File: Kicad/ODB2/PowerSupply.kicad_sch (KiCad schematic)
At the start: 54 parts, among them J2 Batt4v2, J3 Batt7V4, Q3 PJA3411_R1_00001, U2 TPS61201DRCR, U3 LM1085-5.0, U8 MCP1727-1802xMF

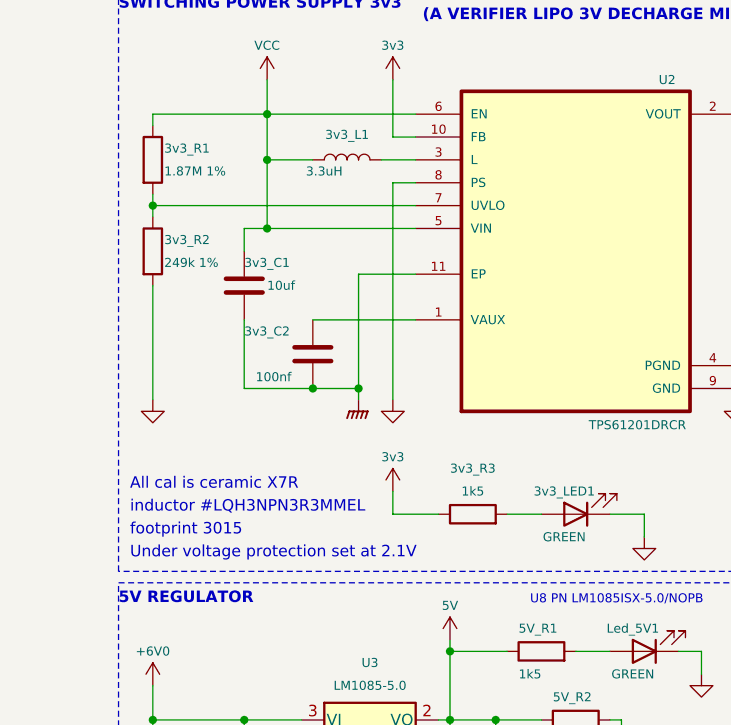
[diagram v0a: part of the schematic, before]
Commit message: fix 3v3_R1 + amp pyros dual channel
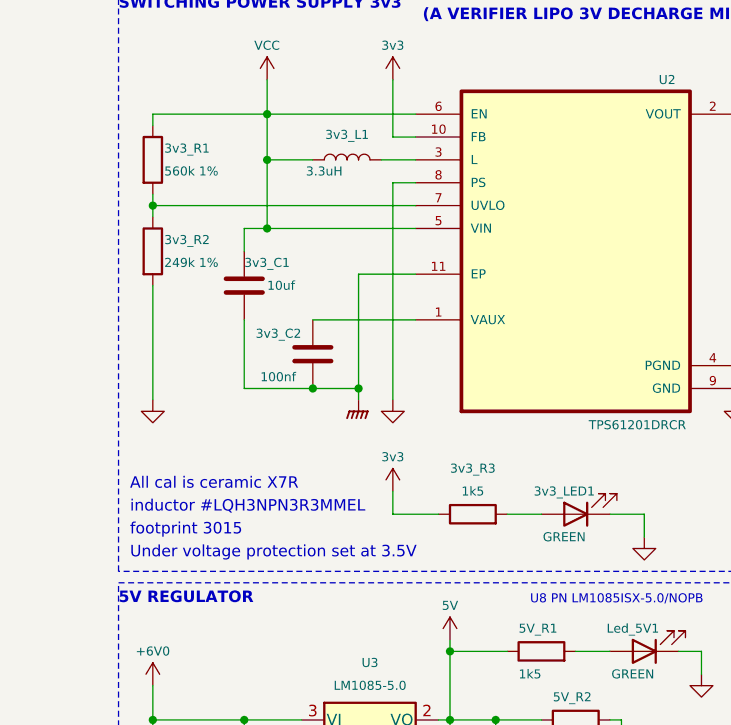
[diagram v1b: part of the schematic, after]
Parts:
- 3v3_R1: value 1.87M 1% -> 560k 1%
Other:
- note added: "Under voltage protection set at 3.5V"
- note removed: "Under voltage protection set at 2.1V"
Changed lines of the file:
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@@
 		)
 	)
-	(text "Under voltage protection set at 2.1V"
+	(text "Under voltage protection set at 3.5V"
 		(exclude_from_sim no)
 		(at 16.51 85.09 0)
@@
 			)
 		)
-		(property "Value" "1.87M 1%"
+		(property "Value" "560k 1%"
 			(at 20.32 41.91 0)
 			(effects
@@
 		(dnp no)
 		(property "Reference" "3v3_C2"
-			(at 29.21 59.69 0)
+			(at 30.48 59.944 0)
 			(effects
 				(font
@@
 		)
 		(property "Value" "100nf"
-			(at 30.48 64.77 0)
-			(effects
-				(font
+			(at 30.988 64.77 0)
+			(effects
+				(font

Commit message: fix amp
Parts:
- 3v3_R1: value 560k 1% -> 3M 1%
- renumbered LED_7v4Enable to LED_7v4Enable1
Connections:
- net +6V0 is gone; now on net +7V4: 5V_C1.1, 5V_C2.1, U3.3 (VI)
- net 3v3 is gone; now on net +3V3: 3v3_C3.1, 3v3_C4.1, 3v3_R3.1, U2.10 (FB), U2.2 (VOUT)
- net 4v2 renamed +3V7
- net 5V renamed +5V
- net 7C4 renamed +7C4
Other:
- note added: "Under voltage protection set at 3.27V"
- note removed: "(A VERIFIER LIPO 3V DECHARGE MINIMAL)"
- note removed: "Under voltage protection set at 3.5V"
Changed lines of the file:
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@@
 		)
 	)
-	(text "Under voltage protection set at 3.5V"
+	(text "Under voltage protection set at 3.27V"
 		(exclude_from_sim no)
 		(at 16.51 85.09 0)
@@
 		)
 	)
-	(text "(A VERIFIER LIPO 3V DECHARGE MINIMAL)"
-		(exclude_from_sim no)
-		(at 49.022 25.4 0)
-		(effects
-			(font
-				(size 1.27 1.27)
-				(thickness 0.254)
-				(bold yes)
-			)
-			(justify left bottom)
-		)
-	)
 	(text "4v2 Input"
 		(exclude_from_sim no)
@@
 			)
 		)
-		(property "Value" "560k 1%"
+		(property "Value" "3M 1%"
 			(at 20.32 41.91 0)
 			(effects
@@
 			)
 		)
-		(property "Value" "3v3"
+		(property "Value" "+3V3"
 			(at 90.17 27.94 0)
 			(effects
@@
 			)
 		)
-		(property "Value" "4v2"
+		(property "Value" "+3V7"
 			(at 49.53 129.54 0)
 			(effects
@@
 			)
 		)
-		(property "Value" "5V"
+		(property "Value" "+5V"
 			(at 52.07 90.17 0)
 			(effects
@@
 			)
 		)
-		(property "Value" "7C4"
+		(property "Value" "+7C4"
 			(at 241.3 22.86 0)
 			(effects
@@
 		)
 		(property "Value" "+1V8"
-			(at 89.662 169.164 0)
+			(at 90.17 170.18 0)
 			(effects
 				(font
@@
 		(on_board yes)
 		(dnp no)
-		(property "Reference" "LED_7v4Enable"
+		(property "Reference" "LED_7v4Enable1"
 			(at 208.28 72.39 0)
 			(effects
@@
 			(project "ODB2"
 				(path "/4b06c5d1-aa8b-48ed-8972-b43a60cfab78/a0dfa29e-ccca-4096-8481-c7e33c67aac5"
-					(reference "LED_7v4Enable")
+					(reference "LED_7v4Enable1")
 					(unit 1)
 				)
@@
 			)
 		)
-		(property "Value" "3v3"
+		(property "Value" "+3V3"
 			(at 45.72 73.66 0)
 			(effects
@@
 			)
 		)
-		(property "Value" "3v3"
+		(property "Value" "+3V3"
 			(at 45.72 27.94 0)
 			(effects
@@
 		)
 		(property "Value" "+3V3"
-			(at 21.336 167.894 0)
+			(at 21.59 167.894 0)
 			(effects
 				(font
@@
 			)
 		)
-		(property "Value" "+6V0"
+		(property "Value" "+7V4"
 			(at 19.05 95.25 0)
 			(effects
@@
 			)
 		)
-		(property "Value" "4v2"
+		(property "Value" "+3V7"
 			(at 90.17 125.73 0)
 			(effects

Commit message: Final fixes
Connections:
- net 4v2_An renamed 3v7_An
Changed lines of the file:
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@@
 		)
 	)
-	(global_label "4v2_An"
+	(global_label "3v7_An"
 		(shape input)
 		(at 30.48 144.78 180)

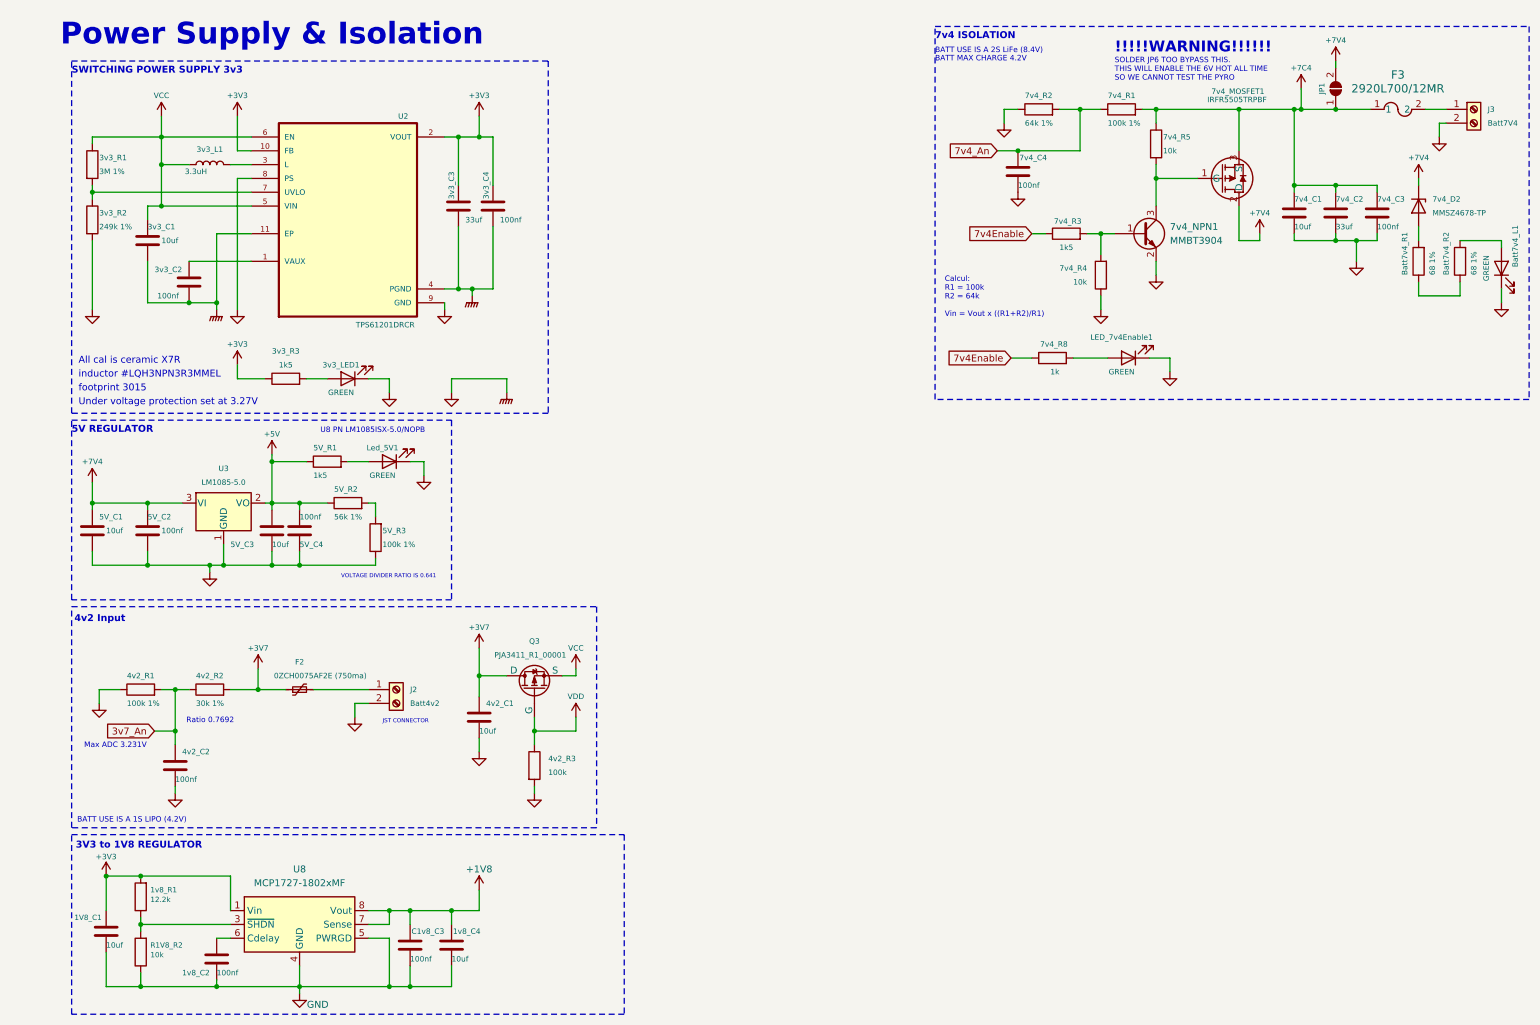
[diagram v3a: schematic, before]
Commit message: fix Labels + fix STM32 projet pinout
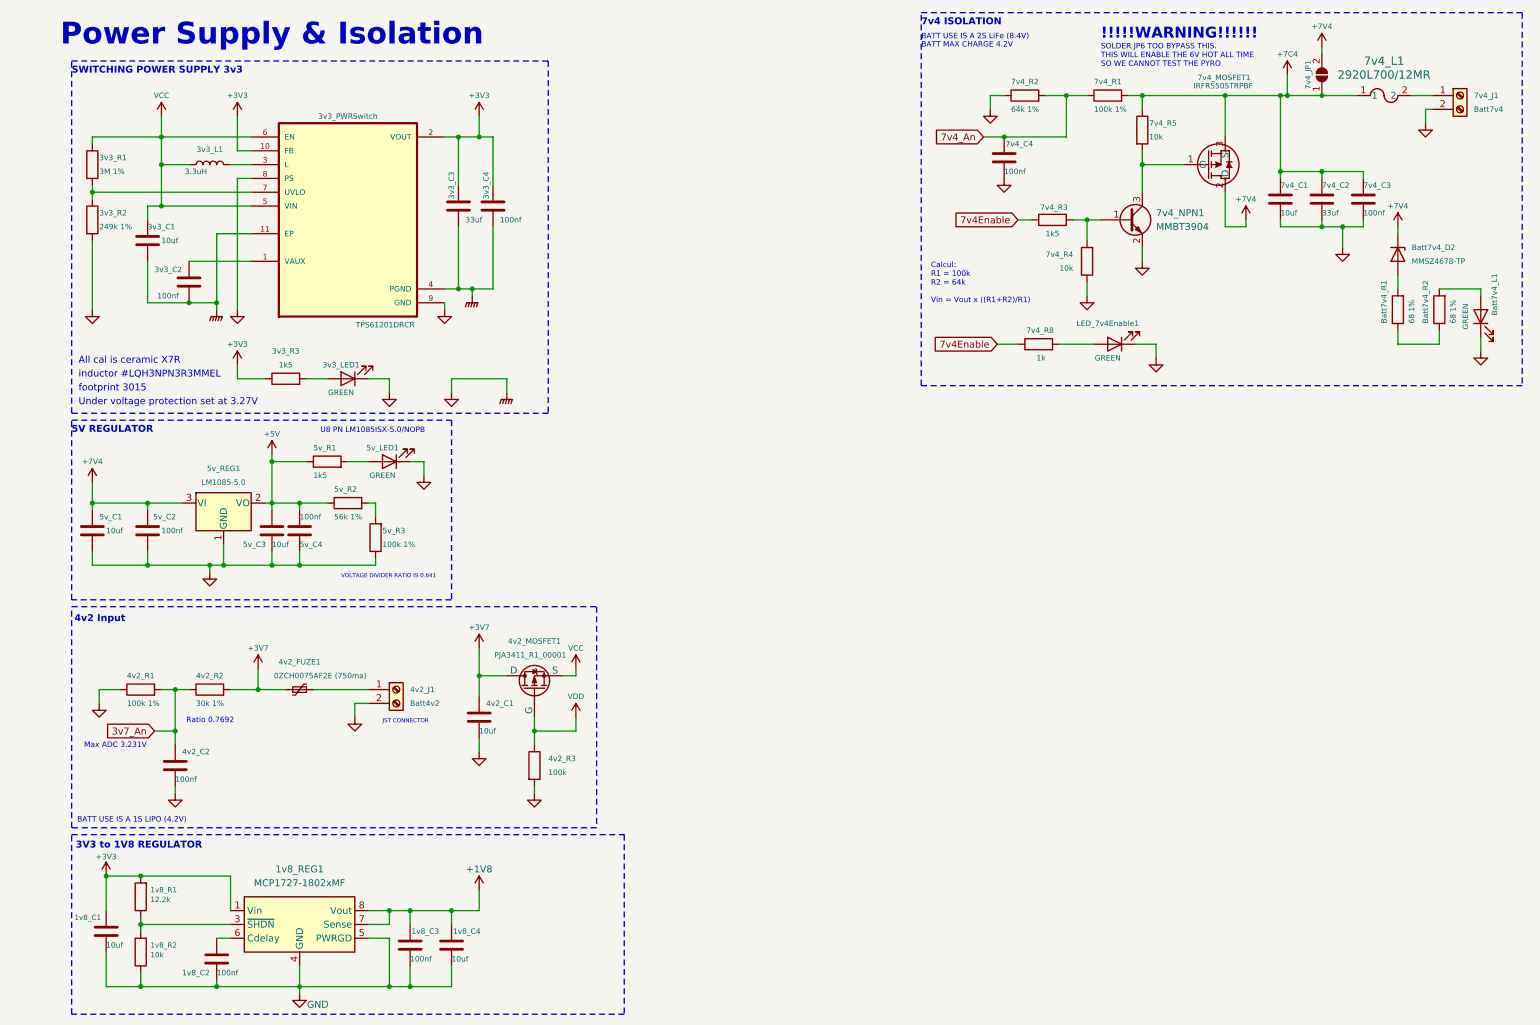
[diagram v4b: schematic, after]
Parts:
- 7v4_J1: renamed from J3; value Batt7V4 -> Batt7v4
- renumbered 1V8_C1 to 1v8_C1, C1v8_C3 to 1v8_C3, R1V8_R2 to 1v8_R2, U8 to 1v8_REG1, U2 to 3v3_PWRSwitch, F2 to 4v2_FUZE1, J2 to 4v2_J1, Q3 to 4v2_MOSFET1, 5V_C1 to 5v_C1, 5V_C2 to 5v_C2, 5V_C3 to 5v_C3, 5V_C4 to 5v_C4, Led_5V1 to 5v_LED1, 5V_R1 to 5v_R1, 5V_R2 to 5v_R2, 5V_R3 to 5v_R3, U3 to 5v_REG1, JP1 to 7v4_JP1, F3 to 7v4_L1, 7v4_D2 to Batt7v4_D2
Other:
- moved on the sheet: 7v4_C1, 7v4_C2, 7v4_C3, 7v4_C4, 7v4_J1, 7v4_JP1, 7v4_L1, 7v4_MOSFET1, 7v4_NPN1, 7v4_R1, 7v4_R2, 7v4_R3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

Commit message: Minor fix et début layout STM et sensors
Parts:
- renumbered 3v3_PWRSwitch to 3v3_PWRSwitch1
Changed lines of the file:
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@@
 		(on_board yes)
 		(dnp no)
-		(property "Reference" "3v3_PWRSwitch"
+		(property "Reference" "3v3_PWRSwitch1"
 			(at 66.04 31.75 0)
 			(effects
@@
 			(project "ODB2"
 				(path "/4b06c5d1-aa8b-48ed-8972-b43a60cfab78/a0dfa29e-ccca-4096-8481-c7e33c67aac5"
-					(reference "3v3_PWRSwitch")
+					(reference "3v3_PWRSwitch1")
 					(unit 1)
 				)

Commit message: Placements composants pcb #1
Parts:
- removed 5v_R2: 56k 1%, Resistor_SMD:R_0805_2012Metric, symbol Device:R
- removed 5v_R3: 100k 1%, Resistor_SMD:R_0805_2012Metric, symbol Device:R
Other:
- note removed: "VOLTAGE DIVIDER RATIO IS 0.641"
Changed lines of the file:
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@@
 	)
 	(junction
-		(at 57.15 114.3)
-		(diameter 0)
-		(color 0 0 0 0)
-	)
-	(junction
-		(at 57.15 102.87)
-		(diameter 0)
-		(color 0 0 0 0)
-	)
-	(junction
 		(at 198.12 27.94)
 		(diameter 0)
@@
 	(wire
 		(pts
-			(xy 71.12 102.87) (xy 71.12 105.41)
-		)
-		(stroke
-			(width 0)
-			(type default)
-		)
-	)
-	(wire
-		(pts
 			(xy 29.21 114.3) (xy 40.64 114.3)
 		)
@@
 	(wire
 		(pts
-			(xy 57.15 114.3) (xy 71.12 114.3)
-		)
-		(stroke
-			(width 0)
-			(type default)
-		)
-	)
-	(wire
-		(pts
 			(xy 201.93 54.61) (xy 201.93 50.8)
 		)
@@
 	(wire
 		(pts
-			(xy 69.85 102.87) (xy 71.12 102.87)
-		)
-		(stroke
-			(width 0)
-			(type default)
-		)
-	)
-	(wire
-		(pts
 			(xy 50.8 102.87) (xy 52.07 102.87)
 		)
@@
 	(wire
 		(pts
-			(xy 57.15 102.87) (xy 62.23 102.87)
-		)
-		(stroke
-			(width 0)
-			(type default)
-		)
-	)
-	(wire
-		(pts
 			(xy 34.29 147.32) (xy 34.29 144.78)
 		)
@@
 	(wire
 		(pts
-			(xy 71.12 114.3) (xy 71.12 113.03)
-		)
-		(stroke
-			(width 0)
-			(type default)
-		)
-	)
-	(wire
-		(pts
 			(xy 52.07 102.87) (xy 57.15 102.87)
 		)
@@
 		)
 	)
-	(text "VOLTAGE DIVIDER RATIO IS 0.641"
-		(exclude_from_sim no)
-		(at 64.77 116.84 0)
-		(effects
-			(font
-				(size 0.75 0.75)
-			)
-			(justify left bottom)
-		)
-	)
 	(text "BATT MAX CHARGE 4.2V"
 		(exclude_from_sim no)
@@
 	)
 	(symbol
-		(lib_id "Device:R")
-		(at 66.04 102.87 90)
-		(unit 1)
-		(exclude_from_sim no)
-		(in_bom yes)
-		(on_board yes)
-		(dnp no)
-		(property "Reference" "5v_R2"
-			(at 63.5 100.33 90)
-			(effects
-				(font
-					(size 1 1)
-				)
-				(justify right)
-			)
-		)
-		(property "Value" "56k 1%"
-			(at 63.5 105.41 90)
-			(effects
-				(font
-					(size 1 1)
-				)
-				(justify right)
-			)
-		)
-		(property "Footprint" "Resistor_SMD:R_0805_2012Metric"
-			(at 66.04 104.648 90)
-			(effects
-				(font
-					(size 1 1)
-				)
-				(hide yes)
-			)
-		)
-		(property "Datasheet" "~"
-			(at 66.04 102.87 0)
-			(effects
-				(font
-					(size 1 1)
-				)
-				(hide yes)
-			)
-		)
-		(property "Description" ""
-			(at 66.04 102.87 0)
-			(effects
-				(font
-					(size 1.27 1.27)
-				)
-				(hide yes)
-			)
-		)
-		(pin "1"
-		)
-		(pin "2"
-		)
-		(instances
-			(project "ODB2"
-				(path "/4b06c5d1-aa8b-48ed-8972-b43a60cfab78/a0dfa29e-ccca-4096-8481-c7e33c67aac5"
-					(reference "5v_R2")
-					(unit 1)
-				)
-			)
-		)
-	)
-	(symbol
 		(lib_id "power:+12C")
 		(at 238.76 24.13 0)
@@
 					(unit 1)
 				)
-			)
-		)
-	)
-	(symbol
-		(lib_id "Device:R")
-		(at 71.12 109.22 180)
-		(unit 1)
-		(exclude_from_sim no)
-		(in_bom yes)
-		(on_board yes)
-		(dnp no)
-		(property "Reference" "5v_R3"
-			(at 72.39 107.95 0)
-			(effects
-				(font
-					(size 1 1)
-				)
-				(justify right)
-			)
-		)
-		(property "Value" "100k 1%"
-			(at 72.39 110.49 0)
-			(effects
-				(font
-					(size 1 1)
-				)
-				(justify right)
-			)
-		)
-		(property "Footprint" "Resistor_SMD:R_0805_2012Metric"
-			(at 72.898 109.22 90)
-			(effects
-				(font
-					(size 1 1)
-				)
-				(hide yes)
-			)
-		)
-		(property "Datasheet" "~"
-			(at 71.12 109.22 0)
-			(effects
-				(font
-					(size 1 1)
-				)
-				(hide yes)
-			)
-		)
-		(property "Description" ""
-			(at 71.12 109.22 0)
-			(effects
-				(font
-					(size 1.27 1.27)
-				)
-				(hide yes)
-			)
-		)
-		(pin "1"
-		)
-		(pin "2"
-		)
-		(instances
-			(project "ODB2"
-				(path "/4b06c5d1-aa8b-48ed-8972-b43a60cfab78/a0dfa29e-ccca-4096-8481-c7e33c67aac5"
-					(reference "5v_R3")
-					(unit 1)
-				)

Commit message: Fix somes issue
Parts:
- 1v8_C1, 1v8_C2, 1v8_C3, 1v8_C4, 3v3_C1, 3v3_C2, 3v3_C3, 3v3_C4, 5v_C1, 5v_C2, 5v_C3, 5v_C4, 7v4_C4: footprint Capacitor_SMD:C_0805_2012Metric -> Capacitor_SMD:C_0603_1608Metric
- 1v8_R1, 1v8_R2, 3v3_R1, 3v3_R2, 3v3_R3, 5v_R1, 7v4_R1, 7v4_R2, 7v4_R3, 7v4_R4, 7v4_R5, 7v4_R8, Batt7v4_R1, Batt7v4_R2: footprint Resistor_SMD:R_0805_2012Metric -> Resistor_SMD:R_0603_1608Metric
- 3v3_LED1, 5v_LED1, Batt7v4_L1, LED_7v4Enable1: footprint LED_SMD:LED_0805_2012Metric -> LED_SMD:LED_0603_1608Metric
- 3v7_C1: renamed from 4v2_C1; footprint Capacitor_SMD:C_0805_2012Metric -> Capacitor_SMD:C_0603_1608Metric
- 3v7_C2: renamed from 4v2_C2; footprint Capacitor_SMD:C_0805_2012Metric -> Capacitor_SMD:C_0603_1608Metric
- 3v7_R1: renamed from 4v2_R1; footprint Resistor_SMD:R_0805_2012Metric -> Resistor_SMD:R_0603_1608Metric
- 3v7_R2: renamed from 4v2_R2; footprint Resistor_SMD:R_0805_2012Metric -> Resistor_SMD:R_0603_1608Metric
- 3v7_R3: renamed from 4v2_R3; footprint Resistor_SMD:R_0805_2012Metric -> Resistor_SMD:R_0603_1608Metric
- 7v4_C1, 7v4_C2, 7v4_C3: footprint Capacitor_SMD:C_1206_3216Metric -> Capacitor_SMD:C_0603_1608Metric
- renumbered 4v2_FUZE1 to 3v7_FUZE1, 4v2_J1 to 3v7_J1, 4v2_MOSFET1 to 3v7_MOSFET1
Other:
- note added: "BATT MAX CHARGE 8.4V"
- note added: "BATT USE IS A 1S LIPO (3.7V)"
- note added: "BATT USE IS A 2S LiFe (7.4V)"
- note added: "Solder JP6 to bypass. This enables 7.4V permanently but disables pyro testing."
- note removed: "BATT USE IS A 1S LIPO (4.2V)"
- note removed: "BATT USE IS A 2S LiFe (8.4V)"
- note removed: "SOLDER JP6 TOO BYPASS THIS. THIS WILL ENABLE THE 6V HOT ALL TIME SO WE CANNOT TEST THE PYRO"
- moved on the sheet: 7v4_C4

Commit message: Updated pcb
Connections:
- net +7C4: no longer names the net of 7v4_C1.1, 7v4_C2.1, 7v4_C3.1, 7v4_JP1.1 (A), 7v4_L1.1, 7v4_MOSFET1.3 (S), 7v4_R1.2, 7v4_R5.1
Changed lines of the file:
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@@
 	)
 	(junction
-		(at 238.76 27.94)
-		(diameter 0)
-		(color 0 0 0 0)
-	)
-	(junction
 		(at 88.9 63.5)
 		(diameter 0)
@@
 	(wire
 		(pts
-			(xy 238.76 24.13) (xy 238.76 27.94)
-		)
-		(stroke
-			(width 0)
-			(type default)
-		)
-	)
-	(wire
-		(pts
 			(xy 259.08 73.66) (xy 259.08 71.12)
 		)
@@
 	(wire
 		(pts
-			(xy 238.76 27.94) (xy 245.11 27.94)
-		)
-		(stroke
-			(width 0)
-			(type default)
-		)
-	)
-	(wire
-		(pts
 			(xy 19.05 46.99) (xy 19.05 45.72)
 		)
@@
 	(wire
 		(pts
-			(xy 237.49 27.94) (xy 238.76 27.94)
+			(xy 237.49 27.94) (xy 245.11 27.94)
 		)
 		(stroke
@@
 					(unit 1)
 				)
-			)
-		)
-	)
-	(symbol
-		(lib_id "power:+12C")
-		(at 238.76 24.13 0)
-		(unit 1)
-		(exclude_from_sim no)
-		(in_bom yes)
-		(on_board yes)
-		(dnp no)
-		(property "Reference" "#PWR028"
-			(at 238.76 27.94 0)
-			(effects
-				(font
-					(size 1 1)
-				)
-				(hide yes)
-			)
-		)
-		(property "Value" "+7C4"
-			(at 238.76 20.32 0)
-			(effects
-				(font
-					(size 1 1)
-				)
-			)
-		)
-		(property "Footprint" ""
-			(at 238.76 24.13 0)
-			(effects
-				(font
-					(size 1 1)
-				)
-				(hide yes)
-			)
-		)
-		(property "Datasheet" ""
-			(at 238.76 24.13 0)
-			(effects
-				(font
-					(size 1 1)
-				)
-				(hide yes)
-			)
-		)
-		(property "Description" ""
-			(at 238.76 24.13 0)
-			(effects
-				(font
-					(size 1.27 1.27)
-				)
-				(hide yes)
-			)
-		)
-		(pin "1"
-		)
-		(instances
-			(project "ODB2"
-				(path "/4b06c5d1-aa8b-48ed-8972-b43a60cfab78/a0dfa29e-ccca-4096-8481-c7e33c67aac5"
-					(reference "#PWR028")
-					(unit 1)
-				)
